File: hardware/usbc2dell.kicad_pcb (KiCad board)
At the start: 2 copper layers, 39.5 x 26.5 mm, 27 parts, among them J1 TYPE-C-31-M-17, J2 DELL_Charger, Q1 MDD50N03D, Q2 MMBT5551, SW1 SW_DIP_x04, U1 ATtiny1616-M, U2 FUSB302BMPX, U3 L7805, U4 SRV05-4

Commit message: move PCB
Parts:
- moved J1 77.5 mm to (23.7, 26.7)
- moved C1 77.5 mm to (29.1, 30.1)
- moved C2 77.5 mm to (30.6, 30.1)
- moved C3 77.5 mm to (37.6, 40.5)
- moved C4 77.5 mm to (34.5, 40.5)
- moved D1 77.5 mm to (52.1, 42.5)
- moved J2 77.5 mm to (49.0, 35.5)
- moved JP1 77.5 mm to (33.8, 30.5)
- moved Q1 77.5 mm to (36.7, 24.9)
- moved Q2 77.5 mm to (41.4, 30.6)
- moved R1 77.5 mm to (36.5, 30.2)
- moved R2 77.5 mm to (57.3, 44.5)
- moved R3 77.5 mm to (57.3, 42.5)
- moved R4 77.5 mm to (57.3, 40.5)
- moved R5 77.5 mm to (40.7, 40.5)
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
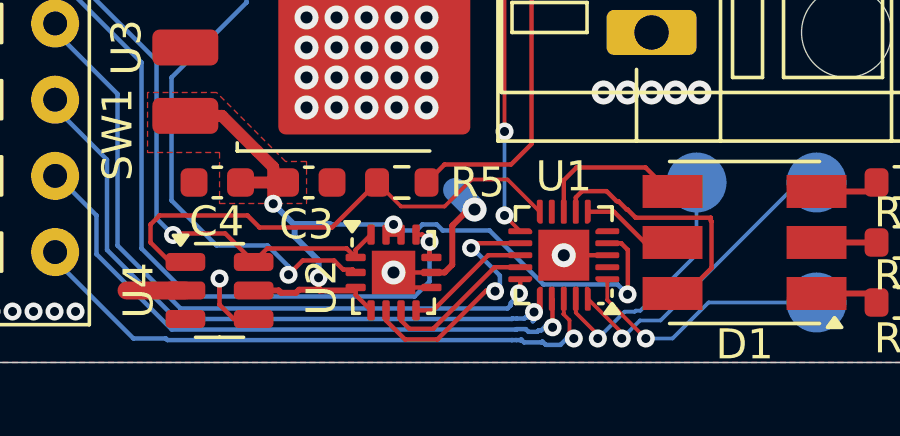
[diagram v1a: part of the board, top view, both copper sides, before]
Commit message: add teardrops
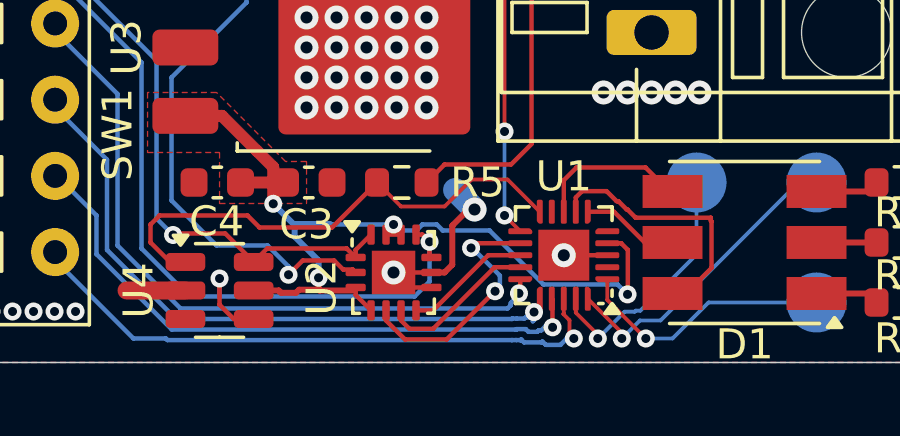
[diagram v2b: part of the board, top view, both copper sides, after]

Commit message: ???
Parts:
- SW1: value SW_DIP_x04 -> DSWB04LHGET

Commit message: DRC
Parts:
- renumbered REF** to HOLE1, REF** to HOLE2, REF** to ICON1, REF** to ICON2

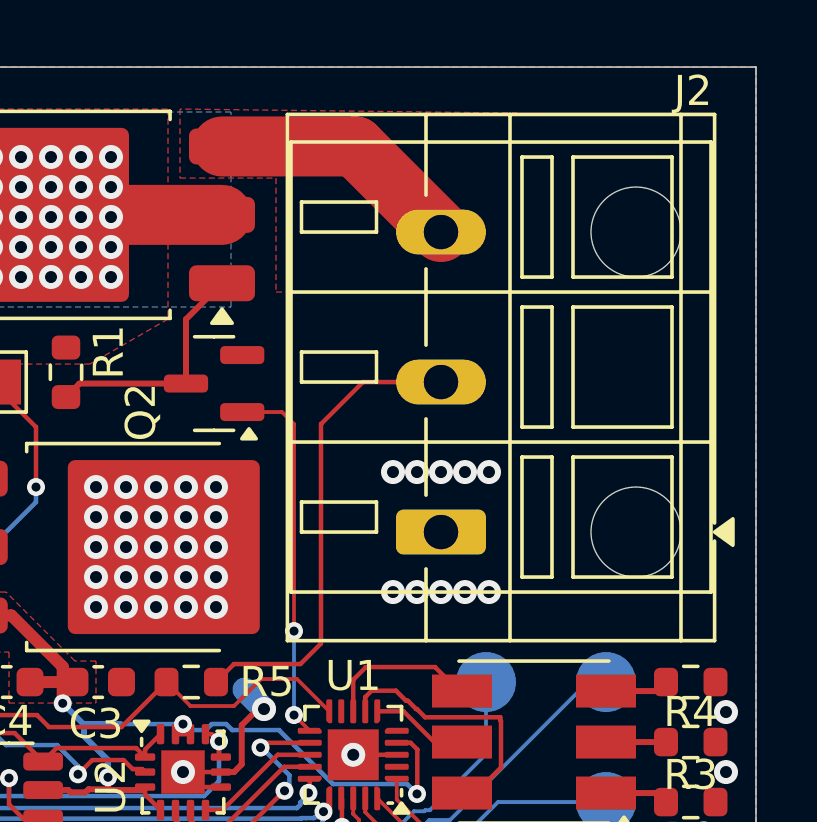
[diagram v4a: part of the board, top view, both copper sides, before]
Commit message: switch to phoenix-style connectors
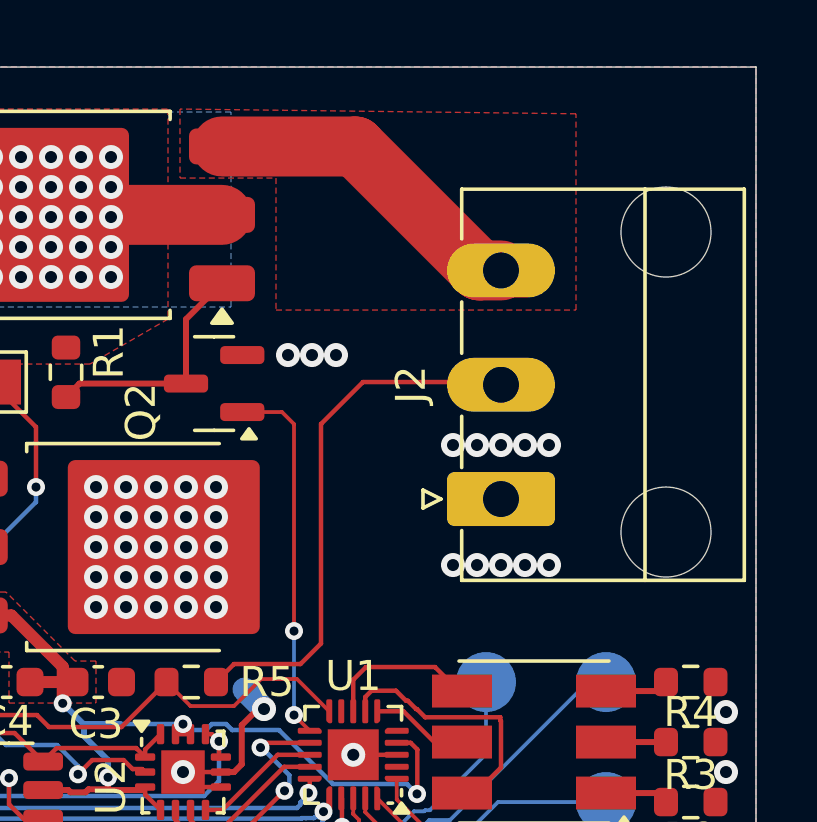
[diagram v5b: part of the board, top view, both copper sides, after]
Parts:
- J2: value DELL_Charger -> WJ15EDGRC-3.81-3P; footprint TerminalBlock_WAGO:TerminalBlock_WAGO_236-103_1x03_P5.00mm_45Degree -> Connector_Phoenix_MC:PhoenixContact_MC_1,5_3-G-3.81_1x03_P3.81mm_Horizontal
- moved J2 2.28 mm to (51.0, 34.4)
- moved HOLE1 1.00 mm to (56.5, 25.5)
- moved HOLE2 1.00 mm to (56.5, 35.5)
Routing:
- net /Vout: track 8.48 -> 11.0 mm
- net /ID_PIN: track 15.9 -> 18.0 mm
- net GND: vias 69 -> 72

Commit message: fix MOSFET
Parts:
- Q1: value MDD50N03D -> Q_PMOS_GDS
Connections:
- Q1 pad 2: VBUS -> /Vout
- Q1 pad 3: /Vout -> VBUS

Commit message: fix mosfet 2
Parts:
- Q1: value Q_PMOS_GDS -> DOD50P06

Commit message: stuff
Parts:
- moved ICON1 0.22 mm to (25.2, 42.6)
